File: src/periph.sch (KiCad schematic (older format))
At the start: 20 parts

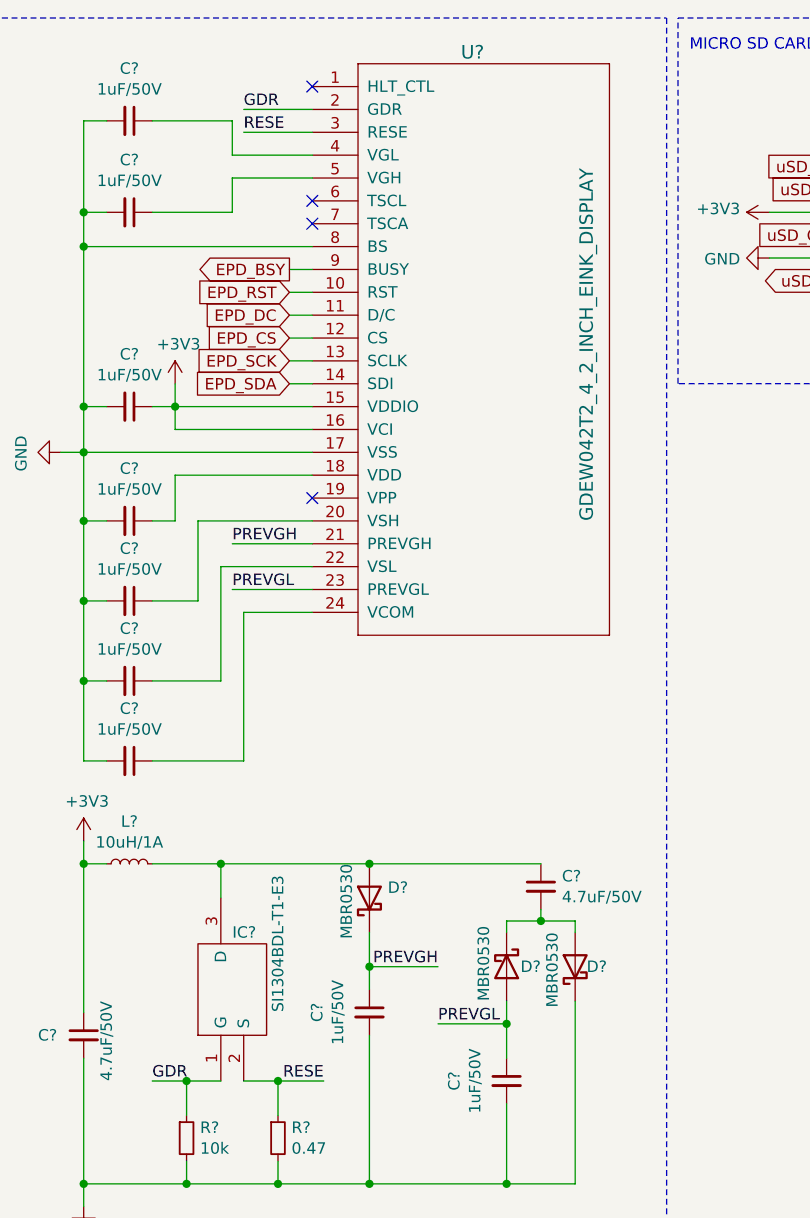
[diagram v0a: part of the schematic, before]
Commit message: fix libraries on macos
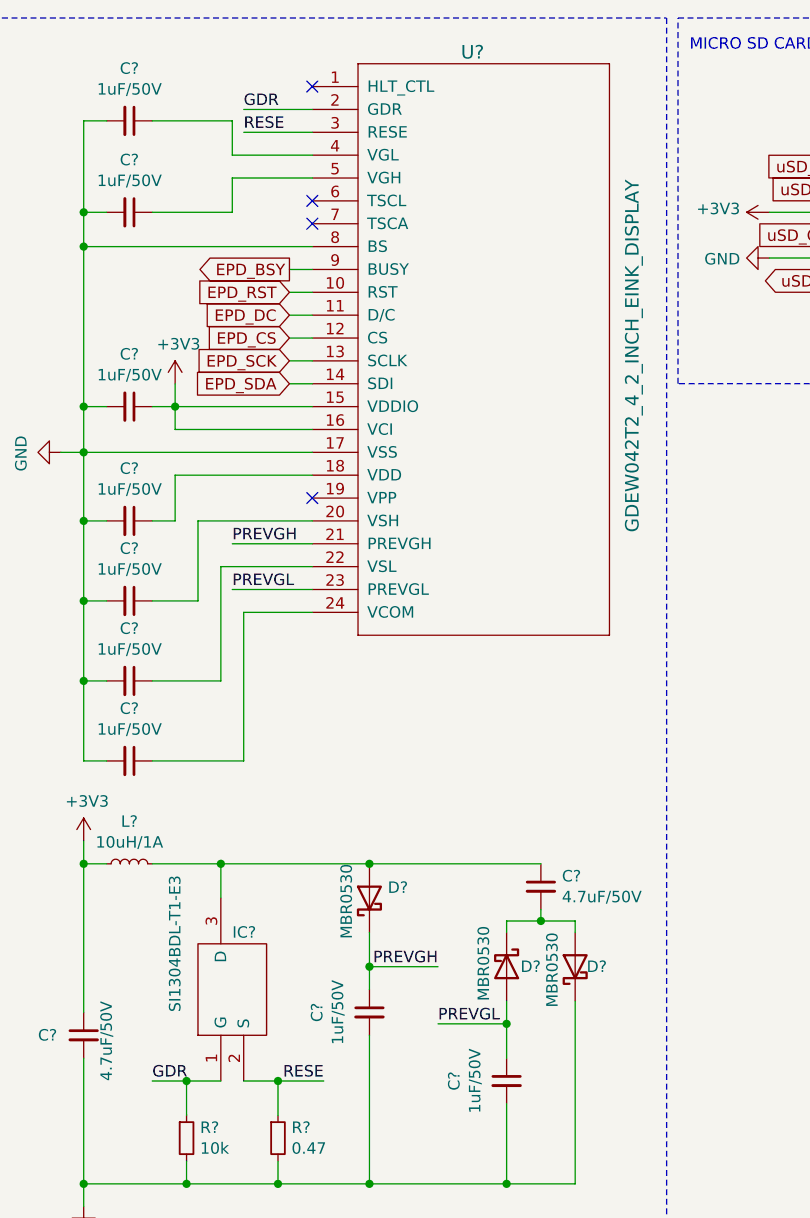
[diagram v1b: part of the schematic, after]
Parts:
- removed IC?: SI1304BDL-T1-E3, SOT65P210X110-3N, symbol SI1304BDL-T1-E3:SI1304BDL-T1-E3
- removed U?: GDEW042T2_4_2_INCH_EINK_DISPLAY, GDEW042T2_FPC, symbol gdew042t2:GDEW042T2_4_2_INCH_EINK_DISPLAY
- added IC?: SI1304BDL-T1-E3, SOT65P210X110-3N, symbol SI1304BDL-T1-E3:SI1304BDL-T1-E3
- added U?: GDEW042T2_4_2_INCH_EINK_DISPLAY, GDEW042T2_FPC, symbol gdew042t2:GDEW042T2_4_2_INCH_EINK_DISPLAY
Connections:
- net +3V3: now also U?.15 (VDDIO), U?.16 (VCI)
- net EPD_BSY: now also U?.9 (BUSY)
- net EPD_CS: now also U?.12 (CS)
- net EPD_DC: now also U?.11 (D/C)
- net EPD_RST: now also U?.10 (RST)
- net EPD_SCK: now also U?.13 (SCLK)
- net EPD_SDA: now also U?.14 (SDI)
- net GDR: now also IC?.1 (G), U?.2 (GDR)
- net GND: now also U?.17 (VSS), U?.8 (BS)
- net PREVGH: now also U?.21 (PREVGH)
- net PREVGL: now also U?.23 (PREVGL)
- net RESE: now also IC?.2 (S), U?.3 (RESE)
- net at C?.1: now also U?.18 (VDD)
- net at C?.1: now also U?.20 (VSH)
- net at C?.1: now also U?.22 (VSL)
- net at C?.1: now also U?.24 (VCOM)
- net at C?.1: now also U?.4 (VGL)
- net at C?.1: now also U?.5 (VGH)
- net at C?.1, D?.2 (A), L?.2: now also IC?.3 (D)
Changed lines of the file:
@@
 Wire Wire Line
 	1900 2500 1300 2500
-$Comp
-L gdew042t2:GDEW042T2_4_2_INCH_EINK_DISPLAY U?
-U 1 1 6177E94D
-P 2100 700
-AR Path="/6177E94D" Ref="U?"  Part="1"
-AR Path="/6177D1DF/6177E94D" Ref="U?"  Part="1"
-F 0 "U?" H 2550 750 59  0000 L CNN
-F 1 "GDEW042T2_4_2_INCH_EINK_DISPLAY" V 3100 -1300 59  0000 L CNN
-F 2 "GDEW042T2_FPC" H 2100 700 50  0001 C CNN
-F 3 "" H 2100 700 50  0001 C CNN
-	1    2100 700
-	1    0    0    -1
-$EndComp
 Wire Wire Line
 	1900 2400 900  2400
@@
 	1    0    0    -1
 $EndComp
-$Comp
-L SI1304BDL-T1-E3:SI1304BDL-T1-E3 IC?
-U 1 1 617CCA8D
-P 1500 5150
-F 0 "IC?" V 2150 5100 50  0000 R CNN
-F 1 "SI1304BDL-T1-E3" H 2400 4900 50  0000 R CNN
-F 2 "SOT65P210X110-3N" H 2150 5250 50  0001 L CNN
-F 3 "http://www.vishay.com/docs/73480/si1304bd.pdf" H 2150 5150 50  0001 L CNN
-F 4 "SI1304BDL-T1-E3, N-channel MOSFET Transistor 0.85 A 30 V, 3-Pin SC-70" H 2150 5050 50  0001 L CNN "Description"
-F 5 "1.1" H 2150 4950 50  0001 L CNN "Height"
-F 6 "Vishay" H 2150 4850 50  0001 L CNN "Manufacturer_Name"
-F 7 "SI1304BDL-T1-E3" H 2150 4750 50  0001 L CNN "Manufacturer_Part_Number"
-F 8 "781-SI1304BDL-E3" H 2150 4650 50  0001 L CNN "Mouser Part Number"
-F 9 "https://www.mouser.com/Search/Refine.aspx?Keyword=781-SI1304BDL-E3" H 2150 4550 50  0001 L CNN "Mouser Price/Stock"
-F 10 "" H 2150 4450 50  0001 L CNN "Arrow Part Number"
-F 11 "" H 2150 4350 50  0001 L CNN "Arrow Price/Stock"
-	1    1500 5150
-	0    -1   -1   0
-$EndComp
 Connection ~ 900  4200
 Wire Wire Line
@@
 Text Notes 3550 650  0    50   ~ 0
 MICRO SD CARD SLOT
+$Comp
+L gdew042t2:GDEW042T2_4_2_INCH_EINK_DISPLAY U?
+U 1 1 617B1130
+P 2100 700
+F 0 "U?" H 2550 750 59  0000 L CNN
+F 1 "GDEW042T2_4_2_INCH_EINK_DISPLAY" V 3300 -1350 59  0000 L CNN
+F 2 "GDEW042T2_FPC" H 2100 700 50  0001 C CNN
+F 3 "" H 2100 700 50  0001 C CNN
+	1    2100 700
+	1    0    0    -1
+$EndComp
+$Comp
+L SI1304BDL-T1-E3:SI1304BDL-T1-E3 IC?
+U 1 1 617B32F2
+P 1500 5150
+F 0 "IC?" V 2150 5100 50  0000 R CNN
+F 1 "SI1304BDL-T1-E3" H 2400 5350 50  0000 R CNN
+F 2 "SOT65P210X110-3N" H 2150 5250 50  0001 L CNN
+F 3 "http://www.vishay.com/docs/73480/si1304bd.pdf" H 2150 5150 50  0001 L CNN
+F 4 "SI1304BDL-T1-E3, N-channel MOSFET Transistor 0.85 A 30 V, 3-Pin SC-70" H 2150 5050 50  0001 L CNN "Description"
+F 5 "1.1" H 2150 4950 50  0001 L CNN "Height"
+F 6 "Vishay" H 2150 4850 50  0001 L CNN "Manufacturer_Name"
+F 7 "SI1304BDL-T1-E3" H 2150 4750 50  0001 L CNN "Manufacturer_Part_Number"
+F 8 "781-SI1304BDL-E3" H 2150 4650 50  0001 L CNN "Mouser Part Number"
+F 9 "https://www.mouser.com/Search/Refine.aspx?Keyword=781-SI1304BDL-E3" H 2150 4550 50  0001 L CNN "Mouser Price/Stock"
+F 10 "" H 2150 4450 50  0001 L CNN "Arrow Part Number"
+F 11 "" H 2150 4350 50  0001 L CNN "Arrow Price/Stock"
+	1    1500 5150
+	0    -1   -1   0
+$EndComp
 $EndSCHEMATC

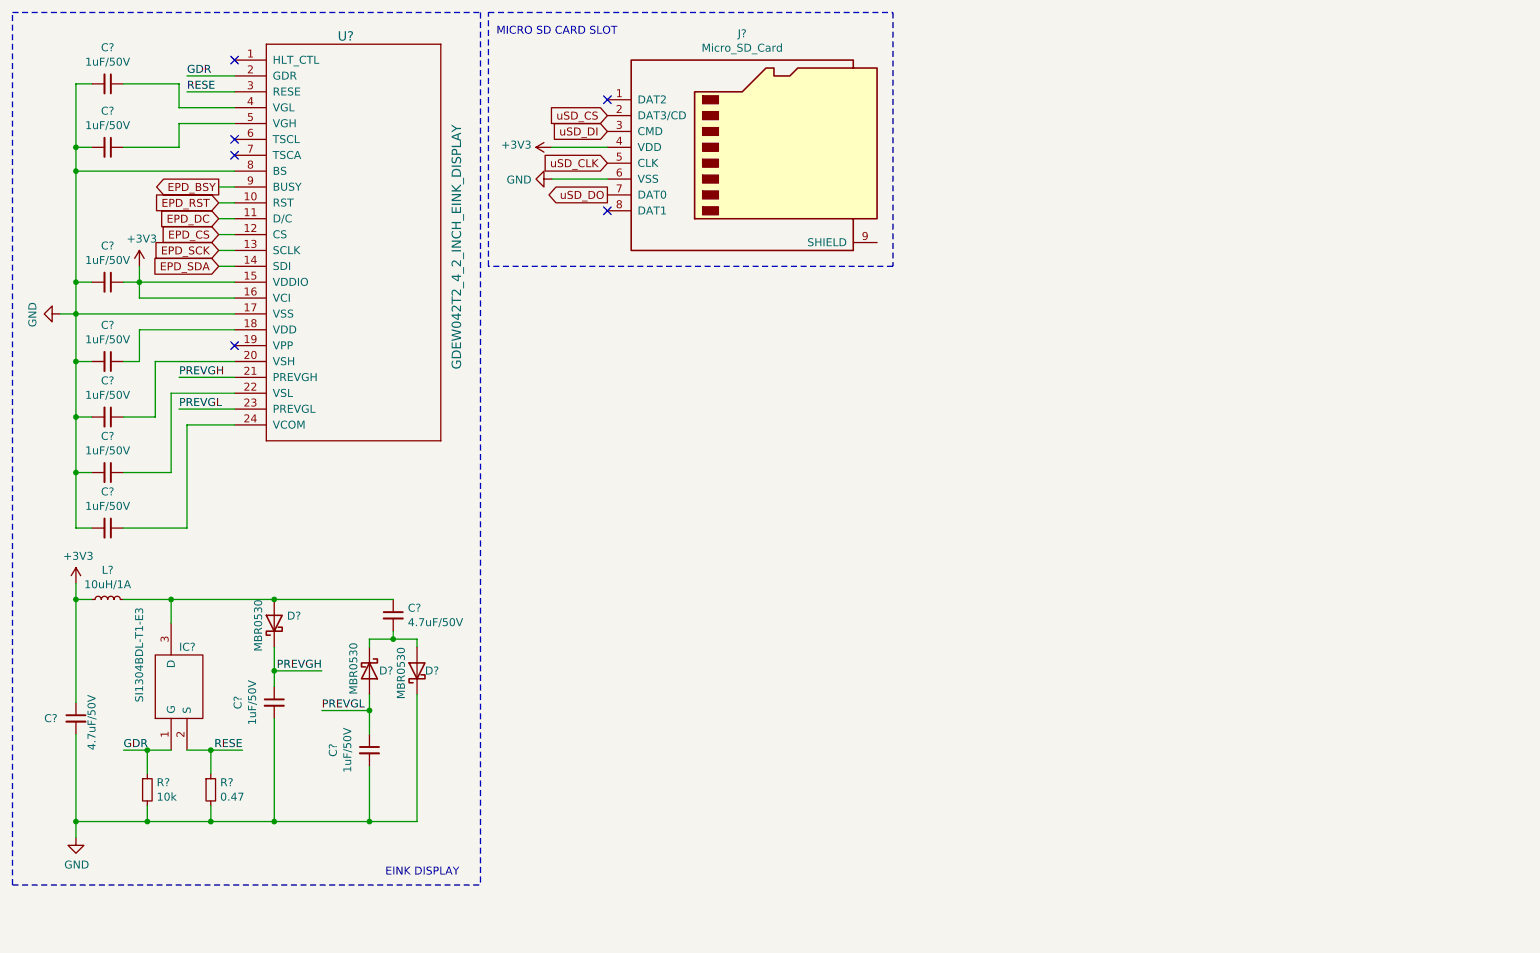
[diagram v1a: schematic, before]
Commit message: switch MCU to STM32G0-series
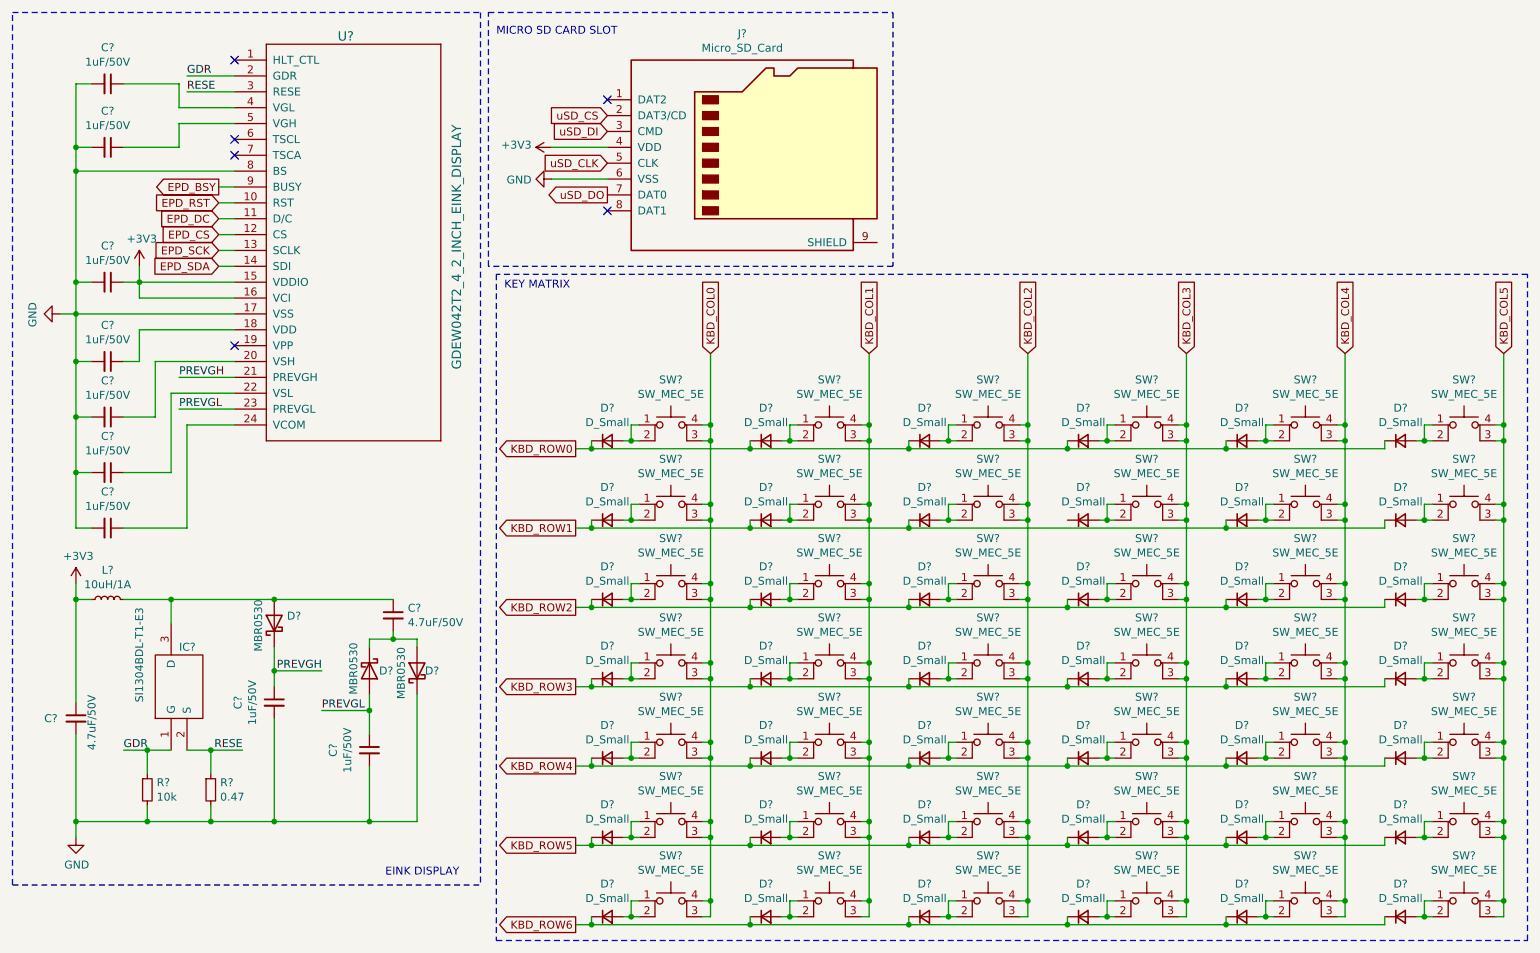
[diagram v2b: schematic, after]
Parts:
- added D? (x42): D_Small, symbol Device:D_Small
- added SW? (x42): SW_MEC_5E, symbol Switch:SW_MEC_5E
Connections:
- new net: D?.2 (A), SW?.1, SW?.2 (x42)
- new net KBD_COL0: SW?.3 (K), SW?.3 (K), SW?.3 (K), SW?.3 (K), SW?.3 (K), SW?.3 (K), SW?.3 (K), SW?.4 (A), SW?.4 (A), SW?.4 (A), SW?.4 (A), SW?.4 (A), SW?.4 (A), SW?.4 (A)
- new net KBD_COL1: SW?.3 (K), SW?.3 (K), SW?.3 (K), SW?.3 (K), SW?.3 (K), SW?.3 (K), SW?.3 (K), SW?.4 (A), SW?.4 (A), SW?.4 (A), SW?.4 (A), SW?.4 (A), SW?.4 (A), SW?.4 (A)
- new net KBD_COL2: SW?.3 (K), SW?.3 (K), SW?.3 (K), SW?.3 (K), SW?.3 (K), SW?.3 (K), SW?.3 (K), SW?.4 (A), SW?.4 (A), SW?.4 (A), SW?.4 (A), SW?.4 (A), SW?.4 (A), SW?.4 (A)
- new net KBD_COL3: SW?.3 (K), SW?.3 (K), SW?.3 (K), SW?.3 (K), SW?.3 (K), SW?.3 (K), SW?.3 (K), SW?.4 (A), SW?.4 (A), SW?.4 (A), SW?.4 (A), SW?.4 (A), SW?.4 (A), SW?.4 (A)
- new net KBD_COL4: SW?.3 (K), SW?.3 (K), SW?.3 (K), SW?.3 (K), SW?.3 (K), SW?.3 (K), SW?.3 (K), SW?.4 (A), SW?.4 (A), SW?.4 (A), SW?.4 (A), SW?.4 (A), SW?.4 (A), SW?.4 (A)
- new net KBD_COL5: SW?.3 (K), SW?.3 (K), SW?.3 (K), SW?.3 (K), SW?.3 (K), SW?.3 (K), SW?.3 (K), SW?.4 (A), SW?.4 (A), SW?.4 (A), SW?.4 (A), SW?.4 (A), SW?.4 (A), SW?.4 (A)
- new net KBD_ROW0: D?.1 (K), D?.1 (K), D?.1 (K), D?.1 (K), D?.1 (K), D?.1 (K)
- new net KBD_ROW1: D?.1 (K), D?.1 (K), D?.1 (K), D?.1 (K), D?.1 (K)
- new net KBD_ROW2: D?.1 (K), D?.1 (K), D?.1 (K), D?.1 (K), D?.1 (K), D?.1 (K)
- new net KBD_ROW3: D?.1 (K), D?.1 (K), D?.1 (K), D?.1 (K), D?.1 (K), D?.1 (K)
- new net KBD_ROW4: D?.1 (K), D?.1 (K), D?.1 (K), D?.1 (K), D?.1 (K), D?.1 (K)
- new net KBD_ROW5: D?.1 (K), D?.1 (K), D?.1 (K), D?.1 (K), D?.1 (K), D?.1 (K)
- new net KBD_ROW6: D?.1 (K), D?.1 (K), D?.1 (K), D?.1 (K), D?.1 (K), D?.1 (K)
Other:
- note added: "KEY MATRIX"
